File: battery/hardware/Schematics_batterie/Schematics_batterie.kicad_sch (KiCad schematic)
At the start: 45 parts, among them IC1 BQ25185DLHR, J1 USB_C_Receptacle_USB2.0_16P, J2 Conn_01x02, J3 Conn_01x02, J4 Conn_ST_STDC14, J5 Conn_01x02, U1 BU33SD5WG-TR, U2 STM32G431KBTx, U3 USBLC6-2SC6

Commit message: derniers branchements et isolation des textes
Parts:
- removed TP10, TP9: TestPoint, TestPoint:TestPoint_Pad_D2.0mm, symbol Connector:TestPoint
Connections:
- net TS MR: now reaches IC1.6 (TS/MR), R3.1, TP6.1
- net LED_play: now reaches D2.1 (K), R7.1
- net Ilim/Vset: now reaches IC1.7 (ILIM/VSET), R6.1, TP7.1
- net Iset: now reaches IC1.8 (ISET), R5.1, TP8.1
- net LED_Stat: now reaches D1.1 (K), R1.1
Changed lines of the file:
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@@
 	)
 	(junction
-		(at 55.88 163.83)
-		(diameter 0)
-		(color 0 0 0 0)
-	)
-	(junction
 		(at 100.33 138.43)
 		(diameter 0)
@@
 	)
 	(junction
-		(at 71.12 163.83)
-		(diameter 0)
-		(color 0 0 0 0)
-	)
-	(junction
 		(at 250.19 154.94)
 		(diameter 0)
@@
 	)
 	(rectangle
-		(start 25.4 26.67)
-		(end 107.95 111.76)
+		(start 20.32 22.86)
+		(end 107.95 113.03)
 		(stroke
 			(width 0)
@@
 		)
 	)
+	(label "Ilim{slash}Vset"
+		(at 82.55 85.09 0)
+		(effects
+			(font
+				(size 1.27 1.27)
+			)
+			(justify left bottom)
+		)
+	)
+	(label "TS MR"
+		(at 80.01 87.63 0)
+		(effects
+			(font
+				(size 1.27 1.27)
+			)
+			(justify left bottom)
+		)
+	)
+	(label "LED_Stat"
+		(at 71.12 172.72 0)
+		(effects
+			(font
+				(size 1.27 1.27)
+			)
+			(justify left bottom)
+		)
+	)
 	(label "VIN"
 		(at 187.96 133.35 0)
@@
 		)
 	)
+	(label "Iset"
+		(at 96.52 83.82 0)
+		(effects
+			(font
+				(size 1.27 1.27)
+			)
+			(justify left bottom)
+		)
+	)
+	(label "LED_play"
+		(at 55.88 171.45 0)
+		(effects
+			(font
+				(size 1.27 1.27)
+			)
+			(justify left bottom)
+		)
+	)
 	(global_label "BAT"
 		(shape input)
@@
 	)
 	(symbol
-		(lib_id "Connector:TestPoint")
-		(at 55.88 163.83 90)
-		(unit 1)
-		(exclude_from_sim no)
-		(in_bom yes)
-		(on_board yes)
-		(dnp no)
-		(fields_autoplaced yes)
-		(property "Reference" "TP9"
-			(at 52.578 158.75 90)
-			(effects
-				(font
-					(size 1.27 1.27)
-				)
-			)
-		)
-		(property "Value" "TestPoint"
-			(at 52.578 161.29 90)
-			(effects
-				(font
-					(size 1.27 1.27)
-				)
-			)
-		)
-		(property "Footprint" "TestPoint:TestPoint_Pad_D2.0mm"
-			(at 55.88 158.75 0)
-			(effects
-				(font
-					(size 1.27 1.27)
-				)
-				(hide yes)
-			)
-		)
-		(property "Datasheet" "~"
-			(at 55.88 158.75 0)
-			(effects
-				(font
-					(size 1.27 1.27)
-				)
-				(hide yes)
-			)
-		)
-		(property "Description" "test point"
-			(at 55.88 163.83 0)
-			(effects
-				(font
-					(size 1.27 1.27)
-				)
-				(hide yes)
-			)
-		)
-		(pin "1"
-		)
-		(instances
-			(project "Schematics_batterie"
-				(path "/4fbe78ef-b629-4e84-bfa0-c62113a81c93"
-					(reference "TP9")
-					(unit 1)
-				)
-			)
-		)
-	)
-	(symbol
 		(lib_id "Device:R_Small")
 		(at 152.4 59.69 270)
@@
 	)
 	(symbol
-		(lib_id "Connector:TestPoint")
-		(at 71.12 163.83 0)
-		(unit 1)
-		(exclude_from_sim no)
-		(in_bom yes)
-		(on_board yes)
-		(dnp no)
-		(property "Reference" "TP10"
-			(at 65.786 154.432 0)
-			(effects
-				(font
-					(size 1.27 1.27)
-				)
-				(justify left)
-			)
-		)
-		(property "Value" "TestPoint"
-			(at 65.786 156.972 0)
-			(effects
-				(font
-					(size 1.27 1.27)
-				)
-				(justify left)
-			)
-		)
-		(property "Footprint" "TestPoint:TestPoint_Pad_D2.0mm"
-			(at 76.2 163.83 0)
-			(effects
-				(font
-					(size 1.27 1.27)
-				)
-				(hide yes)
-			)
-		)
-		(property "Datasheet" "~"
-			(at 76.2 163.83 0)
-			(effects
-				(font
-					(size 1.27 1.27)
-				)
-				(hide yes)
-			)
-		)
-		(property "Description" "test point"
-			(at 71.12 163.83 0)
-			(effects
-				(font
-					(size 1.27 1.27)
-				)
-				(hide yes)
-			)
-		)
-		(pin "1"
-		)
-		(instances
-			(project "Schematics_batterie"
-				(path "/4fbe78ef-b629-4e84-bfa0-c62113a81c93"
-					(reference "TP10")
-					(unit 1)
-				)
-			)
-		)
-	)
-	(symbol
 		(lib_id "power:GND")
 		(at 21.59 102.87 0)
@@
 		)
 		(property "Value" "GND"
-			(at 21.59 107.95 0)
+			(at 25.908 107.442 0)
 			(effects
 				(font

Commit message: FIN DU PCCCBBBBBB
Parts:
- added C12: 100nF, Capacitor_SMD:C_0402_1005Metric, symbol Device:C_Small
- added R8: 9k, Resistor_SMD:R_0603_1608Metric, symbol Device:R_Small
- added R9: 1k, Resistor_SMD:R_0603_1608Metric, symbol Device:R_Small
- D1, D2: footprint LED_SMD:LED_0603_1608Metric_Pad1.05x0.95mm_HandSolder -> LED_SMD:LED_0603_1608Metric
- L1: footprint Inductor_SMD:L_0603_1608Metric_Pad1.05x0.95mm_HandSolder -> Inductor_SMD:L_0603_1608Metric
- R1, R2, R3, R4, R5, R6, R7: footprint Resistor_SMD:R_0603_1608Metric_Pad0.98x0.95mm_HandSolder -> Resistor_SMD:R_0603_1608Metric
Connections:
- net BAT: now also R8.1; no longer J3.1 (Pin_1), J5.1 (Pin_1)
- net GND: now also C12.2, R9.2
- net SYS: now also J3.1 (Pin_1), J5.1 (Pin_1)
- net VBAT: now reaches U2.5 (PA0)
- net VBAT: now also C12.1, R8.2, R9.1
- no-connect marks 19 -> 18

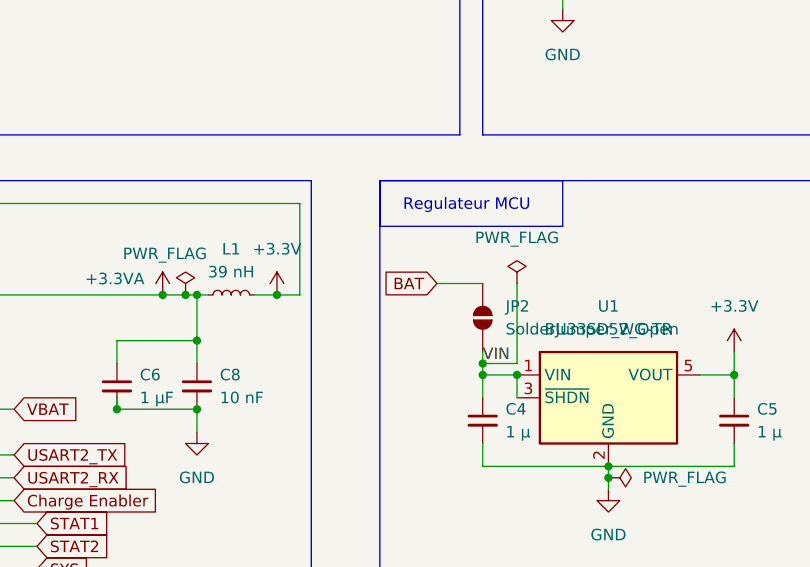
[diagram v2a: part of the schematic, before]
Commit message: il manque encore les gerbers
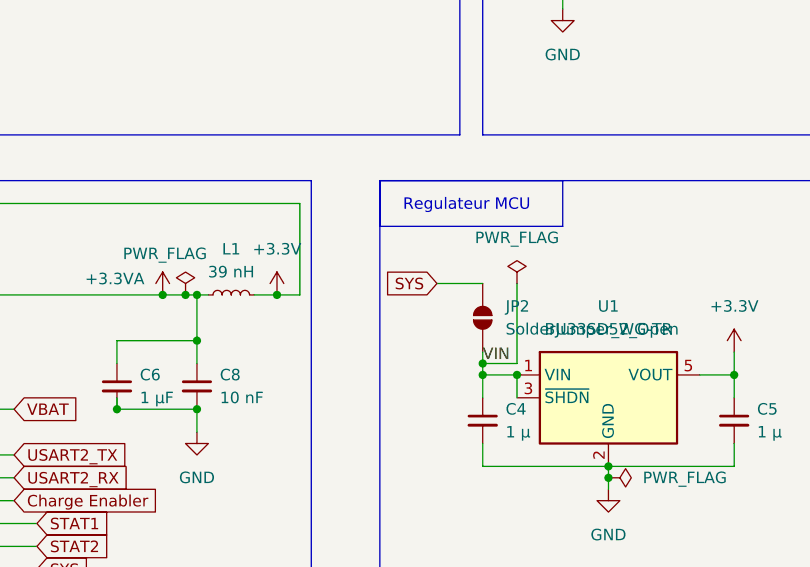
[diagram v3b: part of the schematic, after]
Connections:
- net BAT: no longer JP2.2 (B)
- net SYS: now also JP2.2 (B)
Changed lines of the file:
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@@
 		)
 	)
-	(global_label "BAT"
+	(global_label "SYS"
 		(shape input)
 		(at 182.88 124.46 180)
@@
 		)
 		(property "Intersheetrefs" "${INTERSHEET_REFS}"
-			(at 176.5686 124.46 0)
+			(at 176.3872 124.46 0)
 			(effects
 				(font

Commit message: Commencer la programmation
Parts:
- C11: value 100uF -> 100nF
- R5: value 300 -> 330
- R8: value 9k -> 2k
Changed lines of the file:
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@@
 			)
 		)
-		(property "Value" "100uF"
+		(property "Value" "100nF"
 			(at 92.71 145.034 0)
 			(effects
@@
 			)
 		)
-		(property "Value" "300"
+		(property "Value" "330"
 			(at 94.742 98.298 90)
 			(effects
@@
 			)
 		)
-		(property "Value" "9k"
+		(property "Value" "2k"
 			(at 39.37 135.89 90)
 			(effects
